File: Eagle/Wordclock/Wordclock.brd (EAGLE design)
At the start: 130 x 130 mm, 278 parts, among them IC1 MEGA8-P, Q3 SUP75N06-08

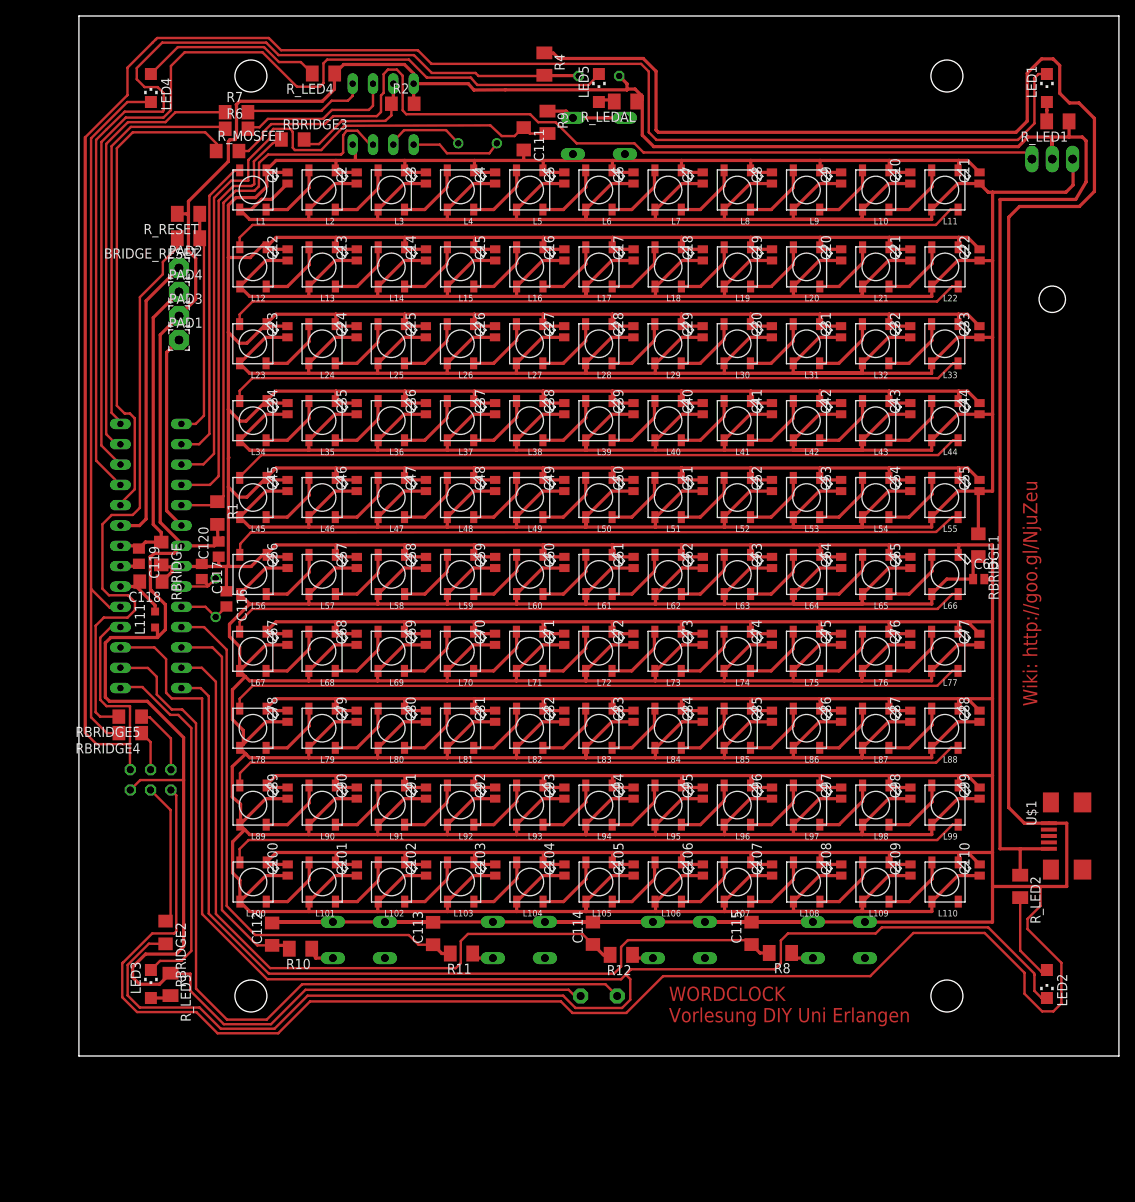
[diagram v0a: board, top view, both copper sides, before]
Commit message: Schutzwiderstand für WS2812 added
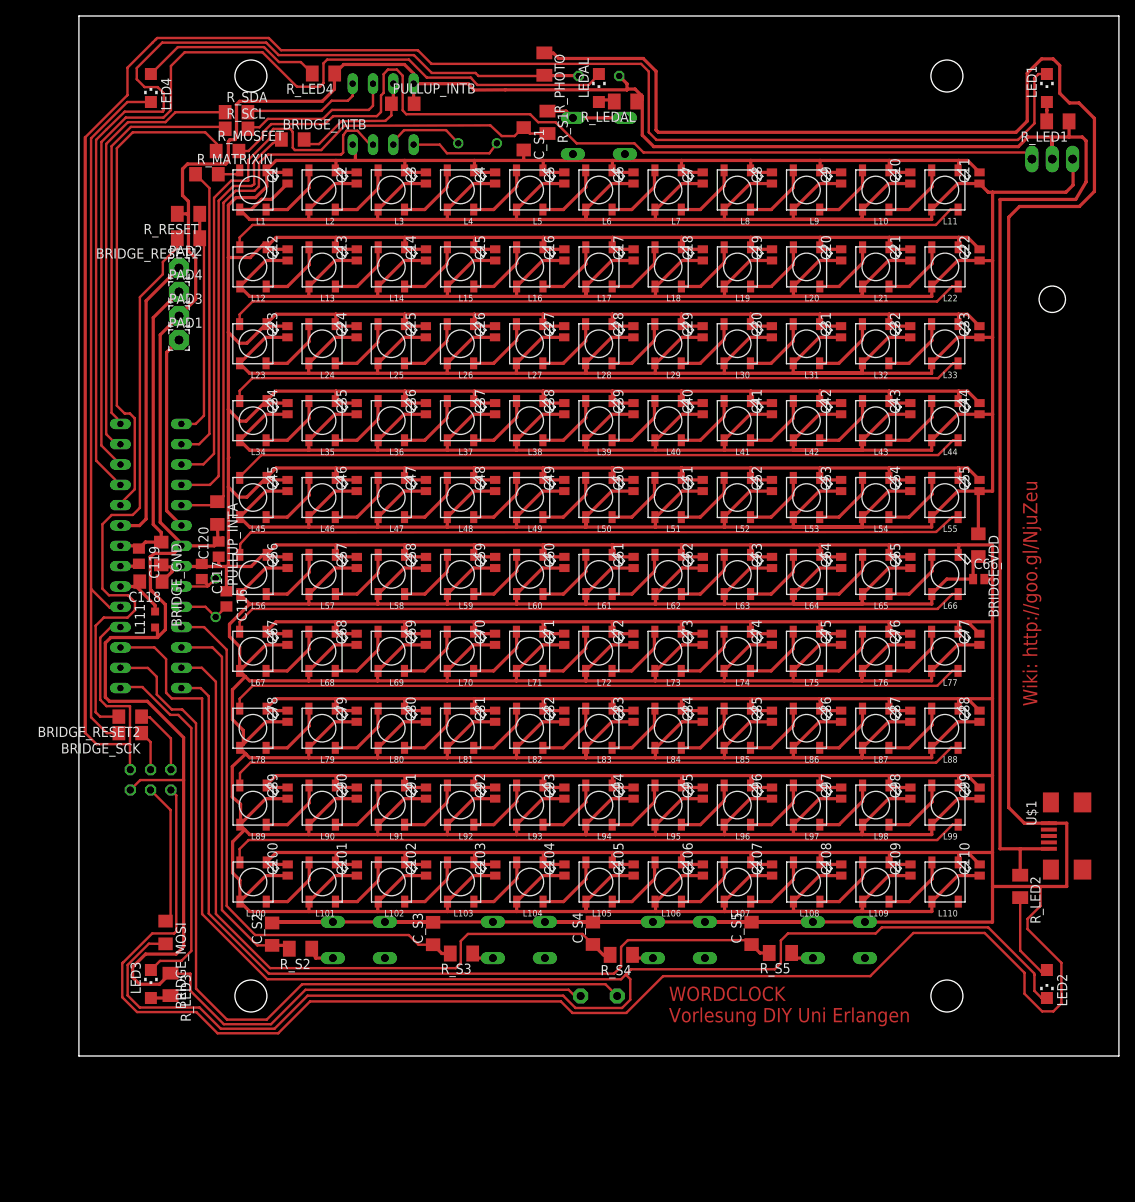
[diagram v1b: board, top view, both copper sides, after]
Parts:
- added R_MATRIXIN: (no value), rcl:R1206
- BRIDGE_GND, BRIDGE_RESET1: value (none) -> 0
- R_RESET: value (none) -> 10k
- renumbered BRIDGE_RESET to BRIDGE_RESET1, C111 to C_S1, C112 to C_S2, C113 to C_S3, C114 to C_S4, C115 to C_S5, LED5 to LEDAL, Q1 to Q_DS, R1 to PULLUP_INTA, R10 to R_S2, R11 to R_S3, R12 to R_S4, R2 to PULLUP_INTB, R4 to R_PHOTO, R6 to R_SCL, R7 to R_SDA, R8 to R_S5, R9 to R_S1, RBRIDGE to BRIDGE_GND, RBRIDGE1 to BRIDGE_VDD, RBRIDGE2 to BRIDGE_MOSI, RBRIDGE3 to BRIDGE_INTB, RBRIDGE4 to BRIDGE_SCK, RBRIDGE5 to BRIDGE_RESET2
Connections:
- new net N$130: L1.4-DIN, R_MATRIXIN.2
- net MATRIXIN: now also R_MATRIXIN.1; no longer L1.4-DIN
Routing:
- net +5V: track 459.1 -> 462.5 mm
- net N$130: track 0.00 -> 2.88 mm
- net MATRIXIN: track 38.9 -> 37.2 mm

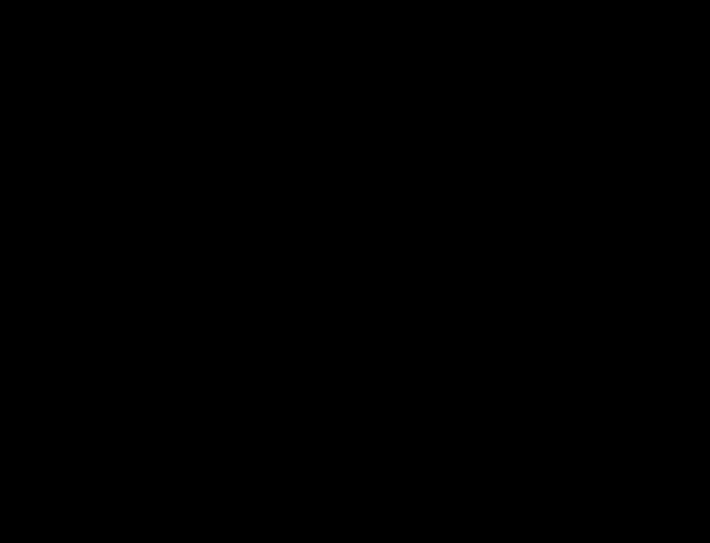
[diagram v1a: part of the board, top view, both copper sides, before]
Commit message: SCL/SDA Pullups hinzugefügt
ACHTUNG!!! Diese Pullups sind auf der ersten Platine noch nicht
enthalten
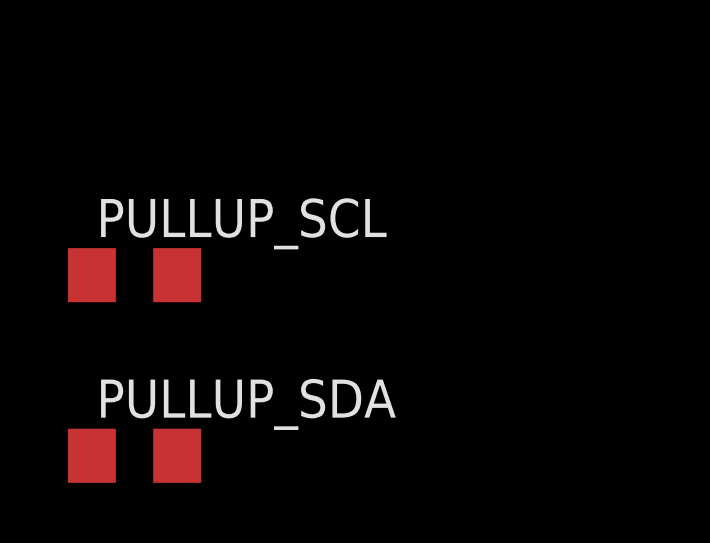
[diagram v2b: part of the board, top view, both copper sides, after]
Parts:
- added PULLUP_SCL, PULLUP_SDA: 4,7k, rcl:R1206
- BRIDGE_INTB, BRIDGE_MOSI, BRIDGE_RESET2, BRIDGE_SCK, BRIDGE_VDD: value (none) -> 0
- C116, C117: value (none) -> 18p
- PULLUP_INTA, PULLUP_INTB: value (none) -> 4,7k
- Q_DS: value (none) -> 32,768MHz
- R_MATRIXIN: value (none) -> 300
- R_MOSFET: value (none) -> 130
- R_S1, R_S2, R_S3, R_S4, R_S5: value (none) -> 1k
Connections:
- net +5V: now also PULLUP_SCL.2, PULLUP_SDA.2
- net N$112: now also PULLUP_SCL.1
- net N$124: now also PULLUP_SDA.1
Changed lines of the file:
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@@
 <elements>
 <element name="S+1" library="eagle-library-edeca.net-v5" package="DIL8" value="DS1337+" x="40.53" y="120.23" rot="MR0"/>
-<element name="Q_DS" library="crystal" package="HC49/S" value="" x="52.33" y="116.59" rot="MR0">
+<element name="Q_DS" library="crystal" package="HC49/S" value="32,768MHz" x="52.33" y="116.59" rot="MR0">
 <attribute name="OC_NEWARK" value="unknown" x="52.33" y="116.59" size="1.778" layer="28" rot="MR0" display="off"/>
 <attribute name="MPN" value="" x="52.33" y="116.59" size="1.778" layer="28" rot="MR0" display="off"/>
@@
 <element name="L110" library="adafruit" package="WS2812B" value="WS2812B" x="110.77" y="24.248903125" rot="R270"/>
 <element name="C110" library="rcl" package="C1310" value="100n" x="115.095" y="25.748903125" rot="R90"/>
-<element name="PULLUP_INTA" library="rcl" package="R1206" value="" x="19.805" y="70.37" rot="R270"/>
-<element name="PULLUP_INTB" library="rcl" package="R1206" value="" x="42.98" y="121.535"/>
+<element name="PULLUP_INTA" library="rcl" package="R1206" value="4,7k" x="19.805" y="70.37" rot="R270"/>
+<element name="PULLUP_INTB" library="rcl" package="R1206" value="4,7k" x="42.98" y="121.535"/>
 <element name="R_LED1" library="rcl" package="M1206" value="" x="124.87" y="119.33" rot="R180"/>
 <element name="R_LED2" library="rcl" package="M1206" value="" x="120.16" y="23.7" rot="R270"/>
@@
 </element>
 <element name="C_S5" library="rcl" package="C1206" value="100n" x="86.58" y="17.83" rot="R90"/>
-<element name="R_S5" library="rcl" package="M1206" value="" x="90.19" y="15.38" rot="R180"/>
+<element name="R_S5" library="rcl" package="M1206" value="1k" x="90.19" y="15.38" rot="R180"/>
 <element name="S1" library="switch-omron" package="B3F-10XX" value="" x="67.5" y="117.5" rot="MR0">
 <attribute name="OC_NEWARK" value="36M3542" x="78.12" y="128.47" size="1.778" layer="28" rot="MR0" display="off"/>
@@
 </element>
 <element name="C_S1" library="rcl" package="C1206" value="100n" x="58.1" y="117.15" rot="R270"/>
-<element name="R_S1" library="rcl" package="M1206" value="" x="61.07" y="119.21" rot="R270"/>
+<element name="R_S1" library="rcl" package="M1206" value="1k" x="61.07" y="119.21" rot="R270"/>
 <element name="S2" library="switch-omron" package="B3F-10XX" value="" x="37.5" y="17" rot="MR180">
 <attribute name="OC_NEWARK" value="36M3542" x="26.88" y="6.03" size="1.778" layer="28" rot="MR180" display="off"/>
@@
 </element>
 <element name="C_S2" library="rcl" package="C1206" value="100n" x="26.65" y="17.73" rot="R90"/>
-<element name="R_S2" library="rcl" package="M1206" value="" x="30.2" y="15.91" rot="R180"/>
+<element name="R_S2" library="rcl" package="M1206" value="1k" x="30.2" y="15.91" rot="R180"/>
 <element name="S3" library="switch-omron" package="B3F-10XX" value="" x="57.5" y="17" rot="MR180">
 <attribute name="OC_NEWARK" value="36M3542" x="36.26" y="7.85" size="1.778" layer="28" rot="MR180" display="off"/>
@@
 </element>
 <element name="C_S3" library="rcl" package="C1206" value="100n" x="46.77" y="17.81" rot="R90"/>
-<element name="R_S3" library="rcl" package="M1206" value="" x="50.32" y="15.31" rot="R180"/>
+<element name="R_S3" library="rcl" package="M1206" value="1k" x="50.32" y="15.31" rot="R180"/>
 <element name="S4" library="switch-omron" package="B3F-10XX" value="" x="77.5" y="17" rot="MR180">
 <attribute name="OC_NEWARK" value="36M3542" x="66.88" y="6.03" size="1.778" layer="28" rot="MR180" display="off"/>
@@
 </element>
 <element name="C_S4" library="rcl" package="C1206" value="100n" x="66.75" y="17.84" rot="R90"/>
-<element name="R_S4" library="rcl" package="M1206" value="" x="70.3" y="15.14" rot="R180"/>
-<element name="C116" library="rcl" package="C0805" value="" x="20.94" y="59.64" rot="R270"/>
-<element name="C117" library="rcl" package="C0805" value="" x="17.86" y="63.06" rot="R270"/>
+<element name="R_S4" library="rcl" package="M1206" value="1k" x="70.3" y="15.14" rot="R180"/>
+<element name="C116" library="rcl" package="C0805" value="18p" x="20.94" y="59.64" rot="R270"/>
+<element name="C117" library="rcl" package="C0805" value="18p" x="17.86" y="63.06" rot="R270"/>
 <element name="SV1" library="con-harting-ml" package="ML6L" value="" x="11.46" y="37.02" rot="MR180">
 <attribute name="OC_NEWARK" value="unknown" x="11.46" y="37.02" size="1.778" layer="28" rot="MR180" display="off"/>
@@
 <element name="PAD4" library="wirepad" package="2,54/1,1" value="" x="15.01" y="98.01"/>
 <element name="BRIDGE_GND" library="rcl" package="R1206" value="0" x="12.79" y="65.31" rot="R270"/>
-<element name="BRIDGE_VDD" library="rcl" package="R1206" value="" x="114.93" y="66.35" rot="R270"/>
-<element name="BRIDGE_INTB" library="rcl" package="R1206" value="" x="29.23" y="117.06"/>
-<element name="R_MOSFET" library="rcl" package="R1206" value="" x="21.08" y="115.62"/>
+<element name="BRIDGE_VDD" library="rcl" package="R1206" value="0" x="114.93" y="66.35" rot="R270"/>
+<element name="BRIDGE_INTB" library="rcl" package="R1206" value="0" x="29.23" y="117.06"/>
+<element name="R_MOSFET" library="rcl" package="R1206" value="130" x="21.08" y="115.62"/>
 <element name="R_SCL" library="rcl" package="R1206" value="" x="22.21" y="118.41"/>
 <element name="R_SDA" library="rcl" package="R1206" value="" x="22.2" y="120.47"/>
 <element name="BRIDGE_RESET1" library="rcl" package="M1206" value="0" x="16.2" y="104.72" rot="R180"/>
-<element name="BRIDGE_MOSI" library="rcl" package="R1206" value="" x="13.33" y="17.94" rot="R270"/>
-<element name="BRIDGE_SCK" library="rcl" package="R1206" value="" x="8.92" y="42.86" rot="R180"/>
-<element name="BRIDGE_RESET2" library="rcl" package="R1206" value="" x="8.91" y="44.92" rot="R180"/>
-<element name="R_MATRIXIN" library="rcl" package="R1206" value="" x="18.5" y="112.72"/>
+<element name="BRIDGE_MOSI" library="rcl" package="R1206" value="0" x="13.33" y="17.94" rot="R270"/>
+<element name="BRIDGE_SCK" library="rcl" package="R1206" value="0" x="8.92" y="42.86" rot="R180"/>
+<element name="BRIDGE_RESET2" library="rcl" package="R1206" value="0" x="8.91" y="44.92" rot="R180"/>
+<element name="R_MATRIXIN" library="rcl" package="R1206" value="300" x="18.5" y="112.72"/>
+<element name="PULLUP_SCL" library="rcl" package="R1206" value="4,7k" x="-2.88" y="-6.85"/>
+<element name="PULLUP_SDA" library="rcl" package="R1206" value="4,7k" x="-2.88" y="-12.87"/>
 </elements>
 <signals>
@@
 <wire x1="16.07" y1="114" x2="20.86" y2="114" width="0.4064" layer="1"/>
 <wire x1="20.86" y1="114" x2="21.18" y2="114.32" width="0.4064" layer="1"/>
+<contactref element="PULLUP_SDA" pad="2"/>
+<contactref element="PULLUP_SCL" pad="2"/>
+<wire x1="-1.458" y1="-6.85" x2="10.08" y2="11.47" width="0" layer="19" extent="1-1"/>
+<wire x1="-1.458" y1="-12.87" x2="-1.458" y2="-6.85" width="0" layer="19" extent="1-1"/>
 </signal>
 <signal name="N$119">
@@
 <wire x1="25.07" y1="118.59" x2="23.702" y2="118.59" width="0.3048" layer="1"/>
 <wire x1="23.702" y1="118.59" x2="23.632" y2="118.41" width="0.3048" layer="1"/>
+<contactref element="PULLUP_SCL" pad="1"/>
+<wire x1="-4.302" y1="-6.85" x2="23.632" y2="118.41" width="0" layer="19" extent="1-1"/>
 </signal>
 <signal name="N$124">
@@
 <wire x1="32.82" y1="120.64" x2="23.682" y2="120.64" width="0.3048" layer="1"/>
 <wire x1="23.682" y1="120.64" x2="23.622" y2="120.47" width="0.3048" layer="1"/>
+<contactref element="PULLUP_SDA" pad="1"/>
+<wire x1="-4.302" y1="-12.87" x2="23.622" y2="120.47" width="0" layer="19" extent="1-1"/>
 </signal>
 <signal name="NC1">

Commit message: weiter Bauteilewerte angepasst
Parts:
- R_SCL, R_SDA: value (none) -> 0
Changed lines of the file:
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@@
 <element name="BRIDGE_INTB" library="rcl" package="R1206" value="0" x="29.23" y="117.06"/>
 <element name="R_MOSFET" library="rcl" package="R1206" value="130" x="21.08" y="115.62"/>
-<element name="R_SCL" library="rcl" package="R1206" value="" x="22.21" y="118.41"/>
-<element name="R_SDA" library="rcl" package="R1206" value="" x="22.2" y="120.47"/>
+<element name="R_SCL" library="rcl" package="R1206" value="0" x="22.21" y="118.41"/>
+<element name="R_SDA" library="rcl" package="R1206" value="0" x="22.2" y="120.47"/>
 <element name="BRIDGE_RESET1" library="rcl" package="M1206" value="0" x="16.2" y="104.72" rot="R180"/>
 <element name="BRIDGE_MOSI" library="rcl" package="R1206" value="0" x="13.33" y="17.94" rot="R270"/>

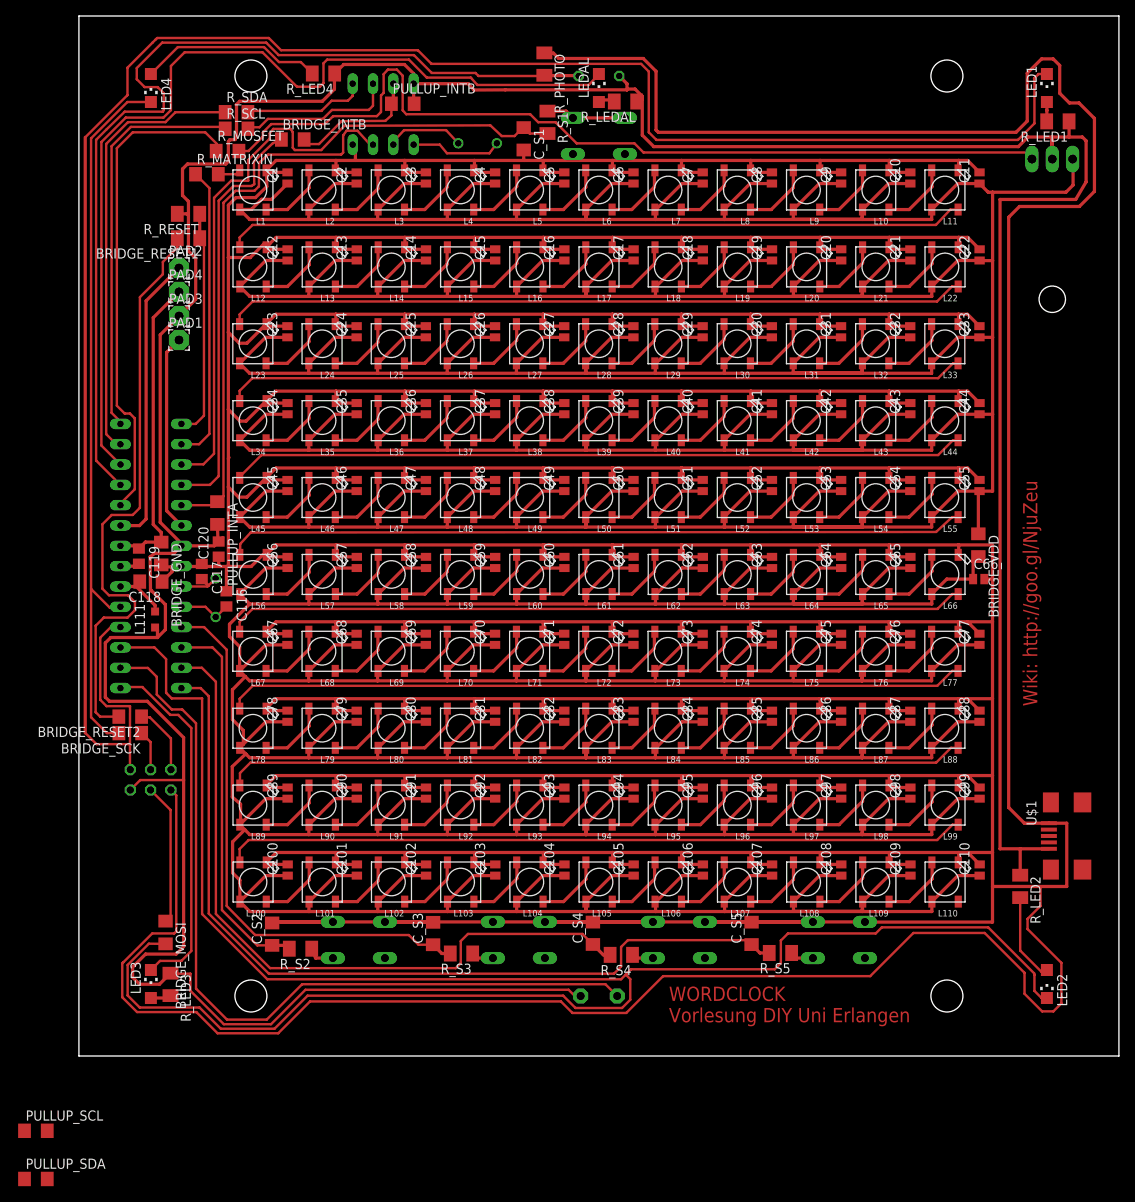
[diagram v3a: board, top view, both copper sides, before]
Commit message: Eagle: Pullups I2C geroutet und Befestigungslöcher auf 3,2 angepasst
Bohrergröße für Platine nun M3 fein nach Tabelle unter
https://de.wikipedia.org/wiki/Metrisches_ISO-Gewinde
Pullup_SCL und Pullup_SDA nun im Layout eingefügt
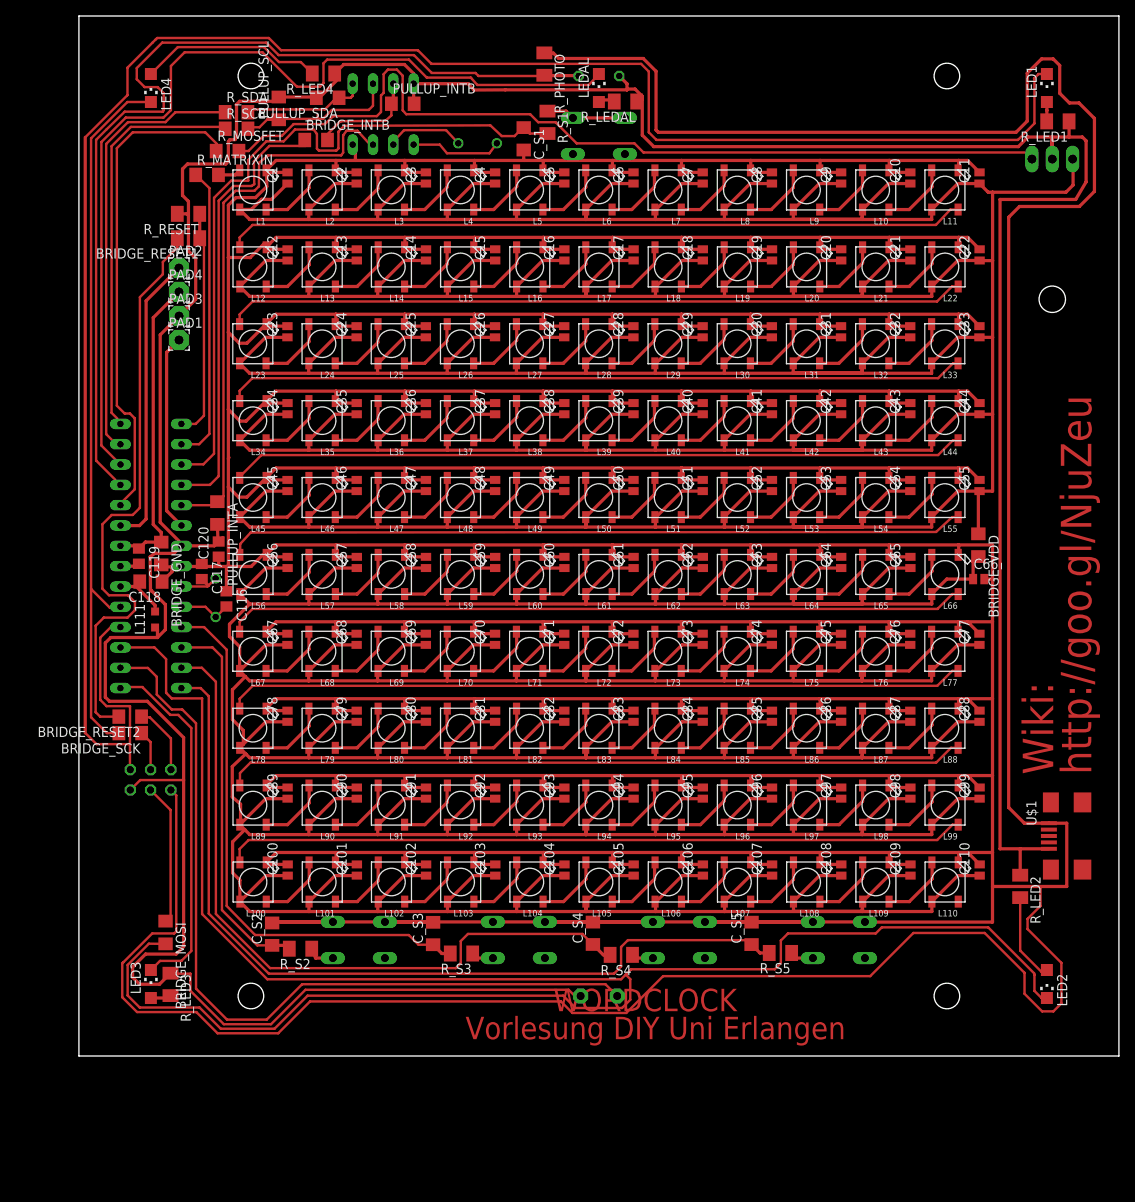
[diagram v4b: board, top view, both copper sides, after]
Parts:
- moved PULLUP_SDA 140.0 mm to (33.6, 122.3), turned to 180 degrees
- moved PULLUP_SCL 131.4 mm to (27.5, 121.0), turned to 90 degrees
- moved BRIDGE_INTB 2.92 mm to (32.1, 117.0)
- moved R_MATRIXIN 0.08 mm to (18.5, 112.6)
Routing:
- net INTB: track 52.1 -> 55.7 mm
- net INTB_UNBRIDGED: track 16.7 -> 13.7 mm
- net N$112: track 19.6 -> 21.6 mm
- net +5V: track 462.5 -> 461.7 mm
- net SCHALTER1: track 88.7 -> 89.4 mm
